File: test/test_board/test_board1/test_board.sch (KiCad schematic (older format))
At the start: 0 parts

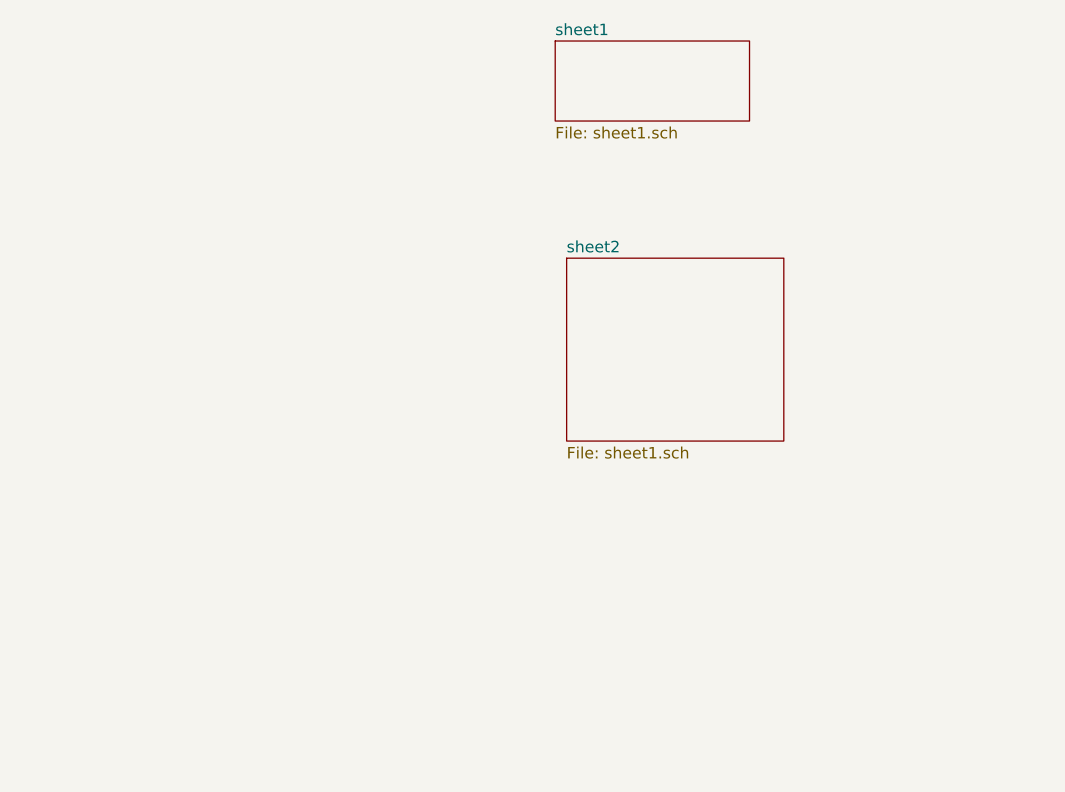
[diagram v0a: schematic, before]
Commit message: Added path to module instances
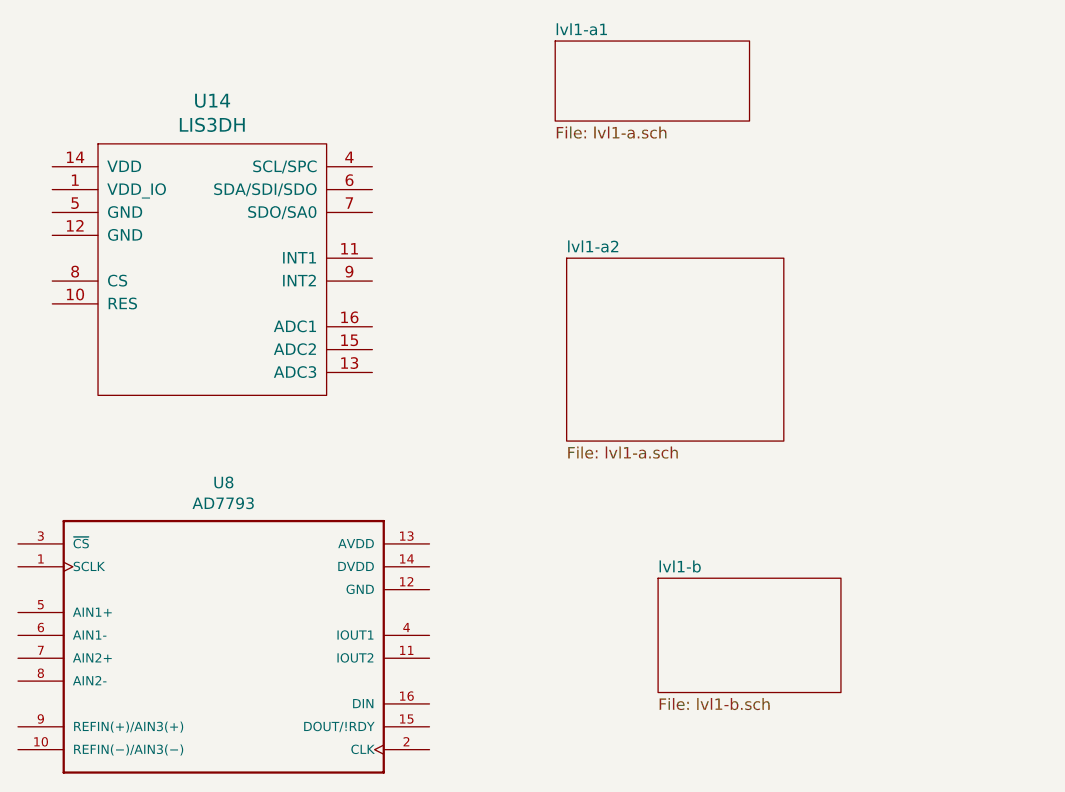
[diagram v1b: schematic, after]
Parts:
- added U14: LIS3DH, symbol accelerometer:LIS3DH
- added U8: AD7793, SOP65P640X120-16N, symbol adc:AD7793
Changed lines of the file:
@@
 $Descr A4 11693 8268
 encoding utf-8
-Sheet 1 3
+Sheet 1 8
 Title ""
 Date ""
@@
 S 3550 1300 850 350
 U 5E6781CF
-F0 "sheet1" 50
-F1 "sheet1.sch" 50
+F0 "lvl1-a1" 50
+F1 "lvl1-a.sch" 50
 $EndSheet
 $Sheet
 S 3600 2250 950 800
 U 5E678707
-F0 "sheet2" 50
-F1 "sheet1.sch" 50
+F0 "lvl1-a2" 50
+F1 "lvl1-a.sch" 50
+$EndSheet
+$Comp
+L accelerometer:LIS3DH U14
+U 1 1 5E67E75F
+P 2050 2300
+F 0 "U14" H 2050 3037 60 0000 C CNN
+F 1 "LIS3DH" H 2050 2931 60 0000 C CNN
+F 2 "" H 1900 2500 60 0001 C CNN
+F 3 "" H 1900 2500 60 0001 C CNN
+1 2050 2300
+1 0 0 -1
+$EndComp
+$Comp
+L adc:AD7793 U8
+U 1 1 5E67EAF2
+P 2100 4000
+F 0 "U8" H 2100 4767 50 0000 C CNN
+F 1 "AD7793" H 2100 4676 50 0000 C CNN
+F 2 "SOP65P640X120-16N" H 2100 4000 50 0001 L BNN
+F 3 "None" H 2100 4000 50 0001 L BNN
+F 4 "Unavailable" H 2100 4000 50 0001 L BNN "Field4"
+F 5 "TSSOP-16 Analog Devices" H 2100 4000 50 0001 L BNN "Field5"
+F 6 "AD7793" H 2100 4000 50 0001 L BNN "Field6"
+F 7 "Triple Channel Single ADC Delta-Sigma 470sps 24-bit Serial 16-Pin TSSOP T/R" H 2100 4000 50 0001 L BNN "Field7"
+F 8 "Analog Devices" H 2100 4000 50 0001 L BNN "Field8"
+1 2100 4000
+1 0 0 -1
+$EndComp
+$Sheet
+S 4000 3650 800 500
+U 5E6EBAF2
+F0 "lvl1-b" 50
+F1 "lvl1-b.sch" 50
 $EndSheet
 $EndSCHEMATC

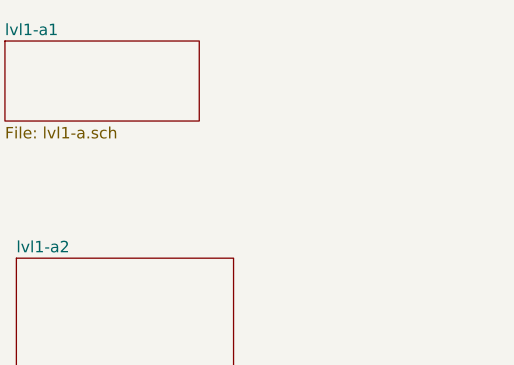
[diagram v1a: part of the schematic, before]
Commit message: Adding some test boards
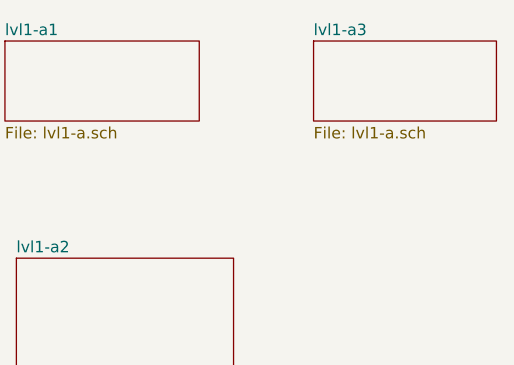
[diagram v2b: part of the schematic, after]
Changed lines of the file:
@@
 $Descr A4 11693 8268
 encoding utf-8
-Sheet 1 8
+Sheet 1 11
 Title ""
 Date ""
@@
 F1 "lvl1-b.sch" 50
 $EndSheet
+$Sheet
+S 4900 1300 800 350
+U 5E6EC0CC
+F0 "lvl1-a3" 50
+F1 "lvl1-a.sch" 50
+$EndSheet
 $EndSCHEMATC

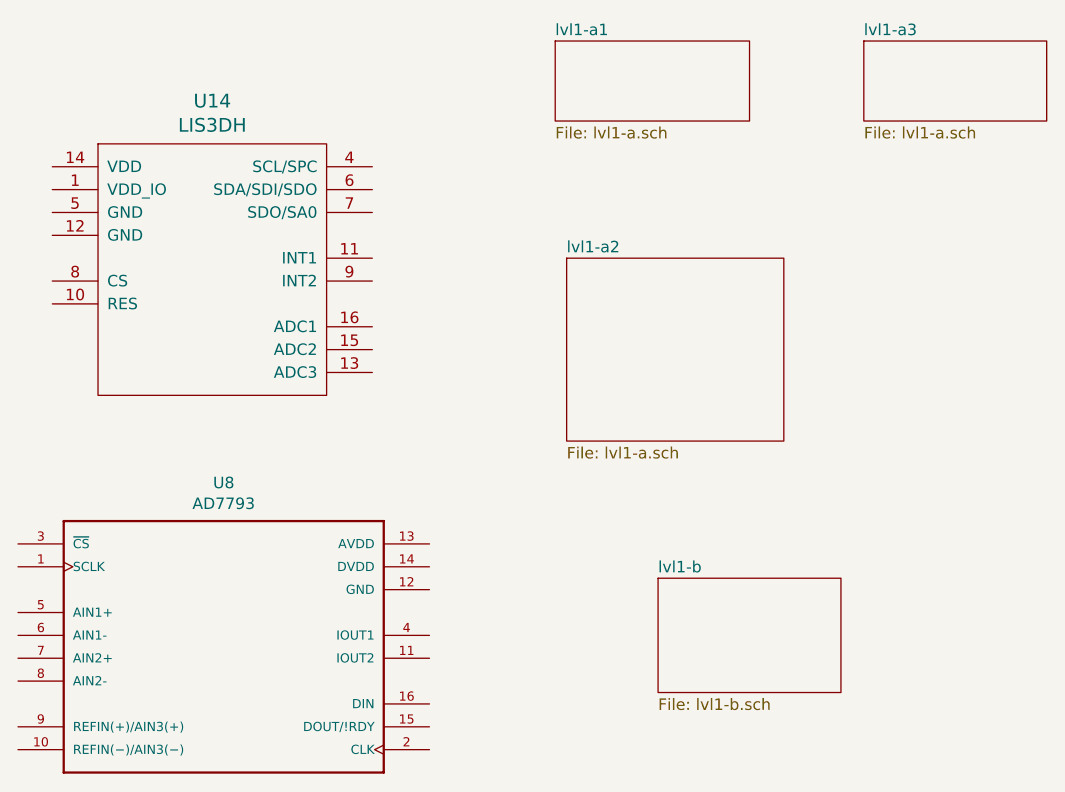
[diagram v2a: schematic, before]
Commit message: Adding schematic editor to associate kicad parts with kipartman parts
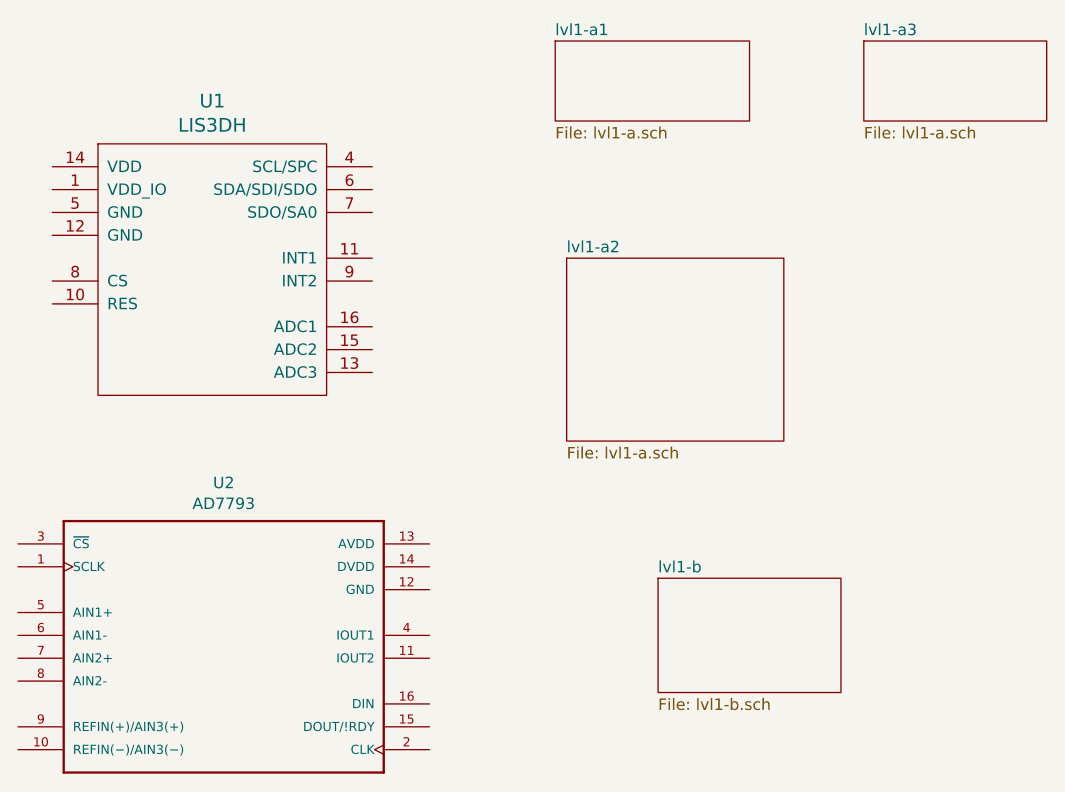
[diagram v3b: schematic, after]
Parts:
- renumbered U14 to U1, U8 to U2
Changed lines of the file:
@@
 $EndDescr
 $Sheet
-S 3550 1300 850 350
+S 3550 1300 850  350
 U 5E6781CF
 F0 "lvl1-a1" 50
@@
 $EndSheet
 $Sheet
-S 3600 2250 950 800
+S 3600 2250 950  800
 U 5E678707
 F0 "lvl1-a2" 50
@@
 $EndSheet
 $Comp
-L accelerometer:LIS3DH U14
+L accelerometer:LIS3DH U1
 U 1 1 5E67E75F
 P 2050 2300
-F 0 "U14" H 2050 3037 60 0000 C CNN
-F 1 "LIS3DH" H 2050 2931 60 0000 C CNN
-F 2 "" H 1900 2500 60 0001 C CNN
-F 3 "" H 1900 2500 60 0001 C CNN
-1 2050 2300
-1 0 0 -1
+F 0 "U1" H 2050 3037 60  0000 C CNN
+F 1 "LIS3DH" H 2050 2931 60  0000 C CNN
+F 2 "" H 1900 2500 60  0001 C CNN
+F 3 "" H 1900 2500 60  0001 C CNN
+	1    2050 2300
+	1    0    0    -1
 $EndComp
 $Comp
-L adc:AD7793 U8
+L adc:AD7793 U2
 U 1 1 5E67EAF2
 P 2100 4000
-F 0 "U8" H 2100 4767 50 0000 C CNN
-F 1 "AD7793" H 2100 4676 50 0000 C CNN
-F 2 "SOP65P640X120-16N" H 2100 4000 50 0001 L BNN
-F 3 "None" H 2100 4000 50 0001 L BNN
-F 4 "Unavailable" H 2100 4000 50 0001 L BNN "Field4"
-F 5 "TSSOP-16 Analog Devices" H 2100 4000 50 0001 L BNN "Field5"
-F 6 "AD7793" H 2100 4000 50 0001 L BNN "Field6"
-F 7 "Triple Channel Single ADC Delta-Sigma 470sps 24-bit Serial 16-Pin TSSOP T/R" H 2100 4000 50 0001 L BNN "Field7"
-F 8 "Analog Devices" H 2100 4000 50 0001 L BNN "Field8"
-1 2100 4000
-1 0 0 -1
+F 0 "U2" H 2100 4767 50  0000 C CNN
+F 1 "AD7793" H 2100 4676 50  0000 C CNN
+F 2 "SOP65P640X120-16N" H 2100 4000 50  0001 L BNN
+F 3 "None" H 2100 4000 50  0001 L BNN
+F 4 "Unavailable" H 2100 4000 50  0001 L BNN "Field4"
+F 5 "TSSOP-16 Analog Devices" H 2100 4000 50  0001 L BNN "Field5"
+F 6 "AD7793" H 2100 4000 50  0001 L BNN "Field6"
+F 7 "Triple Channel Single ADC Delta-Sigma 470sps 24-bit Serial 16-Pin TSSOP T/R" H 2100 4000 50  0001 L BNN "Field7"
+F 8 "Analog Devices" H 2100 4000 50  0001 L BNN "Field8"
+	1    2100 4000
+	1    0    0    -1
 $EndComp
 $Sheet
-S 4000 3650 800 500
+S 4000 3650 800  500
 U 5E6EBAF2
 F0 "lvl1-b" 50
@@
 $EndSheet
 $Sheet
-S 4900 1300 800 350
+S 4900 1300 800  350
 U 5E6EC0CC
 F0 "lvl1-a3" 50

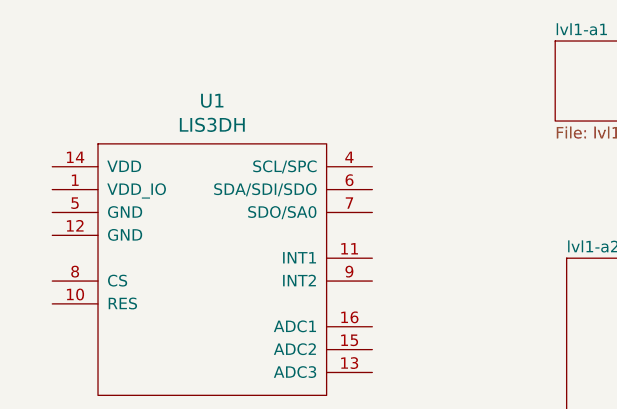
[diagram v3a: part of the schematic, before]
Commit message: Schematic frame working
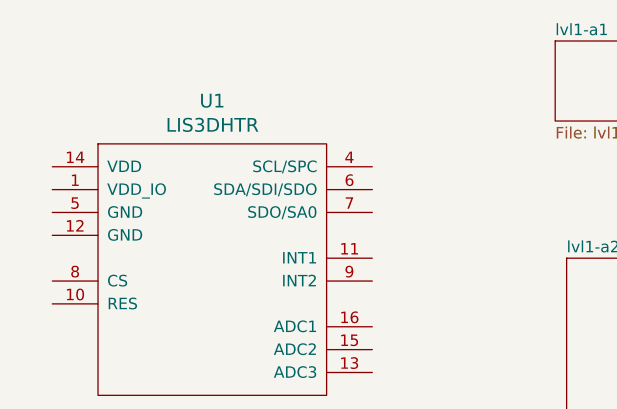
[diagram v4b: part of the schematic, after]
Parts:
- U1: value LIS3DH -> LIS3DHTR; footprint (none) -> LGA:LGA-16; kipart_id (none) -> 51; kipart_sku (none) -> LIS3DHTR
- U2: kipart_id (none) -> 131; kipart_sku (none) -> AD7793
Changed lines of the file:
@@
 $EndDescr
 $Sheet
-S 3550 1300 850  350
+S 3550 1300 850 350
 U 5E6781CF
 F0 "lvl1-a1" 50
@@
 $EndSheet
 $Sheet
-S 3600 2250 950  800
+S 3600 2250 950 800
 U 5E678707
 F0 "lvl1-a2" 50
@@
 U 1 1 5E67E75F
 P 2050 2300
-F 0 "U1" H 2050 3037 60  0000 C CNN
-F 1 "LIS3DH" H 2050 2931 60  0000 C CNN
-F 2 "" H 1900 2500 60  0001 C CNN
-F 3 "" H 1900 2500 60  0001 C CNN
-	1    2050 2300
-	1    0    0    -1
+F 0 "U1" H 2050 3037 60 0000 C CNN
+F 1 "LIS3DHTR" H 2050 2931 60 0000 C CNN
+F 2 "LGA:LGA-16" H 1900 2500 60 0001 C CNN
+F 3 "" H 1900 2500 60 0001 C CNN
+F 4 "51" H 0 0 0 0001 C CNN "kipart_id"
+F 5 "LIS3DHTR" H 0 0 0 0001 C CNN "kipart_sku"
+1 2050 2300
+1 0 0 -1
 $EndComp
 $Comp
@@
 U 1 1 5E67EAF2
 P 2100 4000
-F 0 "U2" H 2100 4767 50  0000 C CNN
-F 1 "AD7793" H 2100 4676 50  0000 C CNN
-F 2 "SOP65P640X120-16N" H 2100 4000 50  0001 L BNN
-F 3 "None" H 2100 4000 50  0001 L BNN
-F 4 "Unavailable" H 2100 4000 50  0001 L BNN "Field4"
-F 5 "TSSOP-16 Analog Devices" H 2100 4000 50  0001 L BNN "Field5"
-F 6 "AD7793" H 2100 4000 50  0001 L BNN "Field6"
-F 7 "Triple Channel Single ADC Delta-Sigma 470sps 24-bit Serial 16-Pin TSSOP T/R" H 2100 4000 50  0001 L BNN "Field7"
-F 8 "Analog Devices" H 2100 4000 50  0001 L BNN "Field8"
-	1    2100 4000
-	1    0    0    -1
+F 0 "U2" H 2100 4767 50 0000 C CNN
+F 1 "AD7793" H 2100 4676 50 0000 C CNN
+F 2 "SOP65P640X120-16N" H 2100 4000 50 0001 L BNN
+F 3 "None" H 2100 4000 50 0001 L BNN
+F 4 "Unavailable" H 2100 4000 50 0001 L BNN "Field4"
+F 5 "TSSOP-16 Analog Devices" H 2100 4000 50 0001 L BNN "Field5"
+F 6 "AD7793" H 2100 4000 50 0001 L BNN "Field6"
+F 7 "Triple Channel Single ADC Delta-Sigma 470sps 24-bit Serial 16-Pin TSSOP T/R" H 2100 4000 50 0001 L BNN "Field7"
+F 8 "Analog Devices" H 2100 4000 50 0001 L BNN "Field8"
+F 9 "131" H 0 0 0 0001 C CNN "kipart_id"
+F 10 "AD7793" H 0 0 0 0001 C CNN "kipart_sku"
+1 2100 4000
+1 0 0 -1
 $EndComp
 $Sheet
-S 4000 3650 800  500
+S 4000 3650 800 500
 U 5E6EBAF2
 F0 "lvl1-b" 50
@@
 $EndSheet
 $Sheet
-S 4900 1300 800  350
+S 4900 1300 800 350
 U 5E6EC0CC
 F0 "lvl1-a3" 50
